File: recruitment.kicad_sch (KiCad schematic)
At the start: 1 part

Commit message: inizio progettazione circuito
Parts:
- removed C1: 1F, Capacitor_SMD:C_0805_2012Metric, symbol Device:C
- added J1: Screw_Terminal_01x01, TerminalBlock:TerminalBlock_Altech_AK300-2_P5.00mm, symbol Connector:Screw_Terminal_01x01
- added K1: Relay_SPST-NO, Relay_THT:Relay_1-Form-A_Schrack-RYII_RM5mm, symbol Relay:Relay_SPST-NO
- added R1, R3, R4: R_US, symbol Device:R_US
- added R2: R_Trim, symbol Device:R_Trim
- added U1: ACS780xLRTR-050B, Sensor_Current:Allegro_PSOF-7_4.8x6.4mm_P1.60mm, symbol Sensor_Current:ACS780xLRTR-050B
- added U2: LM317_TO-220, Package_TO_SOT_THT:TO-220-3_Vertical, symbol Regulator_Linear:LM317_TO-220
- added U3: TL084, symbol Amplifier_Operational:TL084
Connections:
- new net: R1.2, R2.1, U2.1 (ADJ)
- new net: J1.1 (Pin_1), U1.6 (IP-)
- new net: K1.13, U1.5 (IP+)
- new net: U3.1, U3.2 (-)
- new net +3.5V: R3.2, R4.1
- new net +5V: R1.1, U1.1 (VCC), U2.2 (VO), U3.4 (V+)
- new net GND: K1.A2, R2.2, R4.2, U1.2 (GND), U1.4 (NC), U1.7 (NC), U3.11 (V-)
- new net VHall: U1.3 (VOUT), U3.3 (+)
- new net VMonitor: U2.3 (VI)
- new net VPower: K1.14
- no-connect marks 0 -> 2
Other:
- note added: "40 mV/A, ip=0 => Vout = Vcc/2 corrente massima 2.8mA"
- note added: "calcolare r1 r2 in base alla corrente assorbita"
- note added: "scegliendo Vpower = 24Volt"

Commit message: giorno 2 : prime prove e footprint
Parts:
- removed R2: R_Trim, symbol Device:R_Trim
- removed U3: TL084, symbol Amplifier_Operational:TL084
- added R2, R5, R6: R_US, Resistor_THT:R_Axial_DIN0204_L3.6mm_D1.6mm_P2.54mm_Vertical, symbol Device:R_US
- added RV2: R_Potentiometer_US, Potentiometer_THT:Potentiometer_ACP_CA9-H2,5_Horizontal, symbol Device:R_Potentiometer_US
- added U4: OP275, symbol Amplifier_Operational:OP275
- R1, R3, R4: footprint (none) -> Resistor_THT:R_Axial_DIN0204_L3.6mm_D1.6mm_P2.54mm_Vertical
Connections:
- net +5V: now also R6.1, U4.8 (V+)
- net GND: now also R3.2, RV2.2, U4.4 (V-); no longer R4.2
- net VPower: now also R2.1
- net at R1.2, U2.1 (ADJ): now also RV2.1
- net at R3.1: now also R4.1, R2.2, U4.2 (-)
- removed net +3.5V: R3.2, R4.1
- new net: R4.2, R5.2, U4.1
- new net: R5.1, R6.2, U4.3 (+)
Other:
- note added: "11k"
- note added: "120k"
- note added: "2.5Volt per massa virtuale finche l'op non va in saturazione"
- note added: "24-48V"
- note added: "V3 = 2-4V"
- note removed: "40 mV/A, ip=0 => Vout = Vcc/2 corrente massima 2.8mA"
- note removed: "scegliendo Vpower = 24Volt"

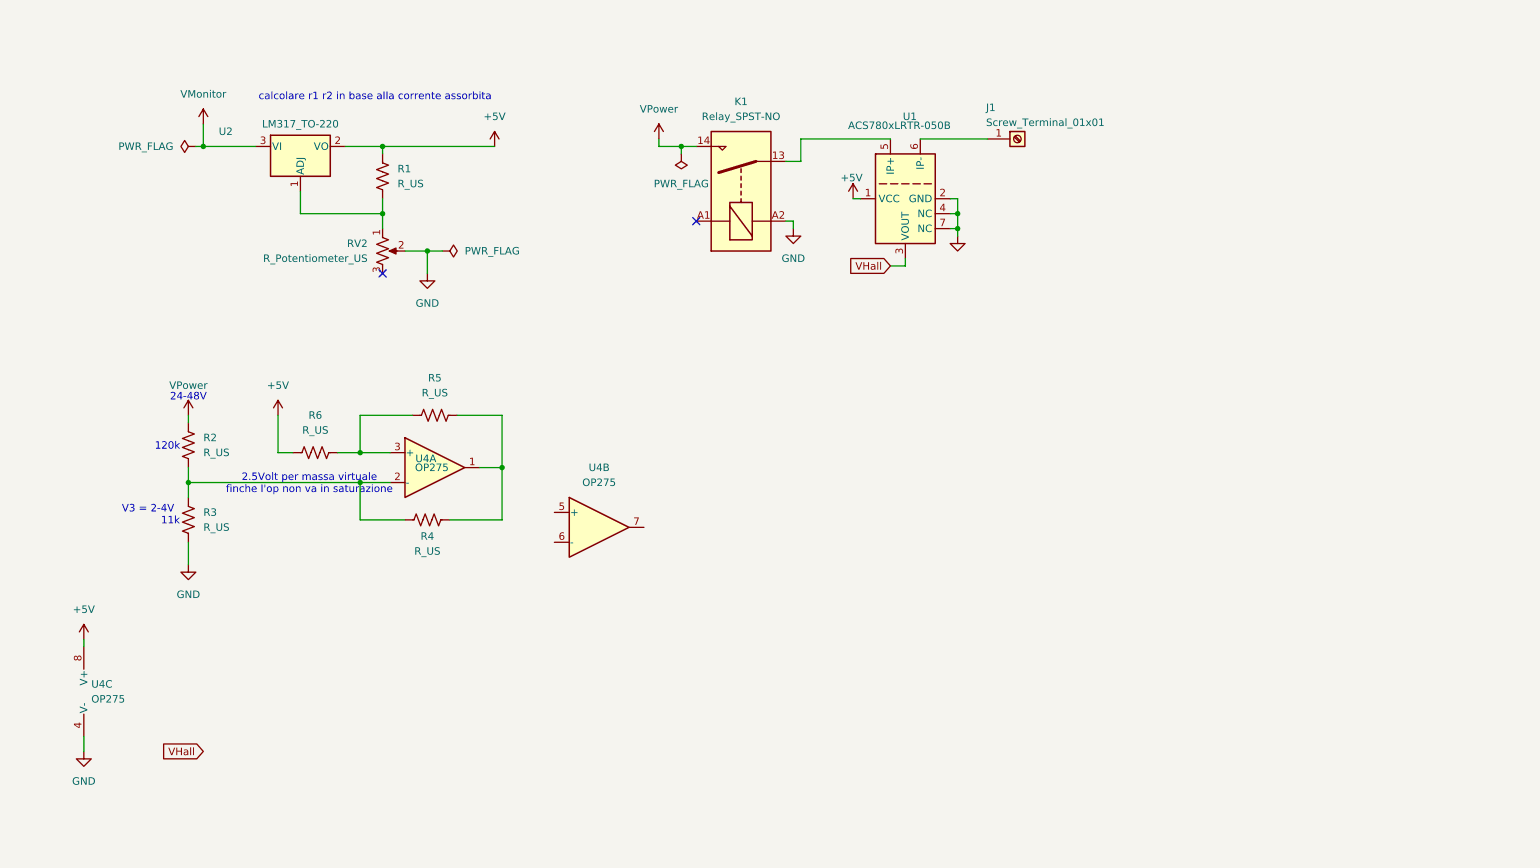
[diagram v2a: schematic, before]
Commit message: continuo schematica, scelta componente latch D
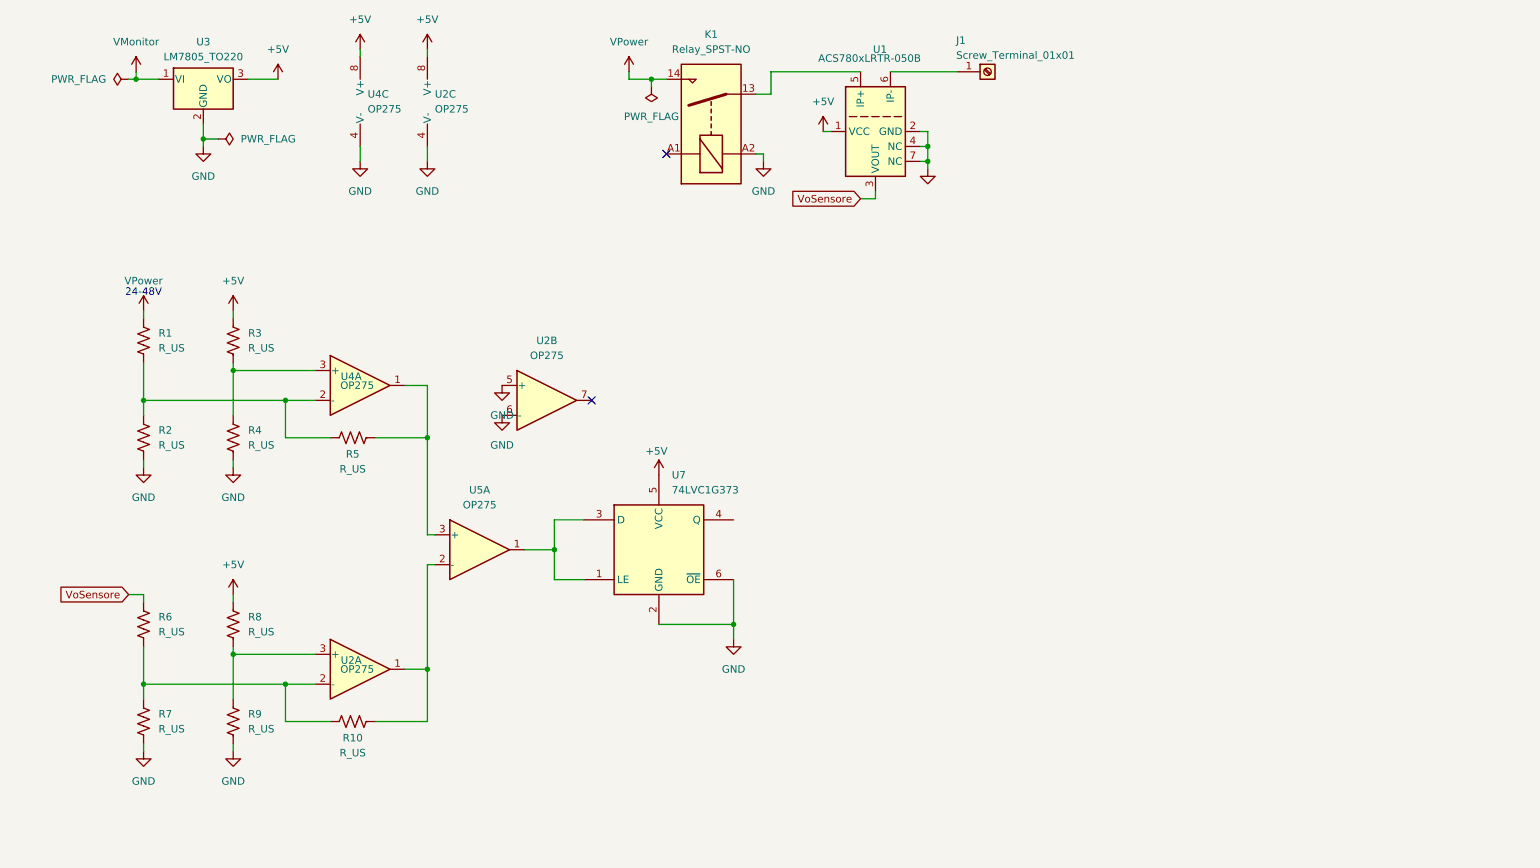
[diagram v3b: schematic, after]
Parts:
- removed R1, R5: R_US, Resistor_THT:R_Axial_DIN0204_L3.6mm_D1.6mm_P2.54mm_Vertical, symbol Device:R_US
- removed RV2: R_Potentiometer_US, Potentiometer_THT:Potentiometer_ACP_CA9-H2,5_Horizontal, symbol Device:R_Potentiometer_US
- removed U2: LM317_TO-220, Package_TO_SOT_THT:TO-220-3_Vertical, symbol Regulator_Linear:LM317_TO-220
- removed unit 2 of U4
- added R10, R4, R6, R7, R8, R9: R_US, Resistor_THT:R_Axial_DIN0204_L3.6mm_D1.6mm_P2.54mm_Vertical, symbol Device:R_US
- added U2, U5: OP275, symbol Amplifier_Operational:OP275
- added U3: LM7805_TO220, Package_TO_SOT_THT:TO-220-3_Vertical, symbol Regulator_Linear:LM7806_TO220
- added U7: 74LVC1G373, symbol 74xGxx:74LVC1G373
- renumbered R2 to R1, R3 to R2, R6 to R3, R4 to R5
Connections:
- net +5V: now also R3.2, R8.2, U2.8 (V+), U3.3 (VO), U7.5 (VCC); no longer R3.1
- net GND: now also R4.2, R7.2, R9.2, U2.4 (V-), U2.5 (+), U2.6 (-), U3.2 (GND), U7.2 (GND), U7.6 (~{OE})
- net VMonitor: now also U3.1 (VI)
- net at R5.2, U4.1: now also U5.3 (+)
- net at U4.3 (+): now also R3.1, R4.1; no longer R3.2
- net VHall renamed VoSensore
- net VoSensore: now also R6.1
- new net: R10.2, U2.1, U5.2 (-)
- new net: R10.1, R6.2, R7.1, U2.2 (-)
- new net: R8.1, R9.1, U2.3 (+)
- new net: U5.1, U7.1 (LE), U7.3 (D)
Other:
- note removed: "11k"
- note removed: "120k"
- note removed: "2.5Volt per massa virtuale finche l'op non va in saturazione"
- note removed: "V3 = 2-4V"
- note removed: "calcolare r1 r2 in base alla corrente assorbita"
- moved on the sheet: J1, K1, R1, R2, R3, R5, U1, U4A, U4C

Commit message: prima prova pcb
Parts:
- removed J1: Screw_Terminal_01x01, TerminalBlock:TerminalBlock_Altech_AK300-2_P5.00mm, symbol Connector:Screw_Terminal_01x01
- removed K1: Relay_SPST-NO, Relay_THT:Relay_1-Form-A_Schrack-RYII_RM5mm, symbol Relay:Relay_SPST-NO
- removed U5: OP275, symbol Amplifier_Operational:OP275
- added J1, J2: ~, TerminalBlock:TerminalBlock_Altech_AK300-2_P5.00mm, symbol Connector:Screw_Terminal_01x02
- added K1: Panasonic_ALFG2PF091, Relay_THT:Relay_SPST_Panasonic_ALFG_FormA_CircularHoles, symbol Relay:Panasonic_ALFG2PF091
- added Q1: IRF9540N, Package_TO_SOT_THT:TO-220-3_Vertical, symbol Transistor_FET:IRF9540N
- added Q2: BC337, Package_TO_SOT_THT:TO-92_Inline, symbol Transistor_BJT:BC337
- added Q3: BC327, Package_TO_SOT_THT:TO-92_Inline, symbol Transistor_BJT:BC327
- added R11, R12, R13, R14: 10k, Resistor_SMD:R_1206_3216Metric, symbol Device:R_US
- added RT1: 10k, Potentiometer_THT:Potentiometer_ACP_CA6-H2,5_Horizontal, symbol Device:R_Potentiometer_Trim_US
- added unit 2 of U3
- R1, R10, R2, R3, R4, R5, R6, R7, R8, R9: footprint Resistor_THT:R_Axial_DIN0204_L3.6mm_D1.6mm_P2.54mm_Vertical -> Resistor_SMD:R_1206_3216Metric
- U2: footprint (none) -> Package_SO:SOIC-8_3.9x4.9mm_P1.27mm
- U3: renamed from U4; footprint (none) -> Package_SO:SOIC-8_3.9x4.9mm_P1.27mm
- U4: renamed from U7; footprint (none) -> Package_TO_SOT_SMD:SOT-23-6
- renumbered U1 to S1, U3 to U1
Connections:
- net GND: now also K1.A2, Q2.3 (E), R13.2, RT1.1; no longer U2.5 (+), U2.6 (-)
- net VMonitor: now also Q1.3 (S), Q3.3 (E), R11.2
- net at R5.2, U3.1: now also U2.5 (+)
- net Load: now reaches S1.6 (IP-)
- net Load: now also J2.2 (Pin_2)
- net at R10.2, U2.1: now also U2.6 (-)
- net at S1.5 (IP+): now also K1.11
- net at U4.1 (LE), U4.3 (D): now also U2.7
- net Shutdown: now reaches U4.4 (Q)
- net Shutdown: now also R12.2
- net VPower renamed Power
- net Power: now also J1.1 (Pin_1), K1.14
- new net: RT1.2, U3.5 (+)
- new net: Q3.1 (C), R13.1, U3.6 (-)
- new net: R14.2, U3.7
- new net: Q2.1 (C), Q3.2 (B), R11.1
- new net: Q2.2 (B), R12.1
- new net: J1.2 (Pin_2), J2.1 (Pin_1)
- new net: Q1.1 (G), R14.1
- new net relé_bobina: K1.A1, Q1.2 (D), RT1.3
- no-connect marks 2 -> 0
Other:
- moved on the sheet: R1, R10, R2, R3, R4, R5, R6, R7, R8, R9, S1, U1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

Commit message: V1.0.0 : prima versione (si spera) funzionante
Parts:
- R1: value R_US -> 120k
- R10: value R_US -> 51k
- R2: value R_US -> 11k
- R3: value R_US -> 6.8k
- R4, R5, R6: value R_US -> 10k
- R7: value R_US -> 51
- R8, R9: value R_US -> 20k
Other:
- title: Template -> Test d'ingresso
- moved on the sheet: J1, J2, K1, Q1, Q2, Q3, R11, R12, R13, R14, RT1, S1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

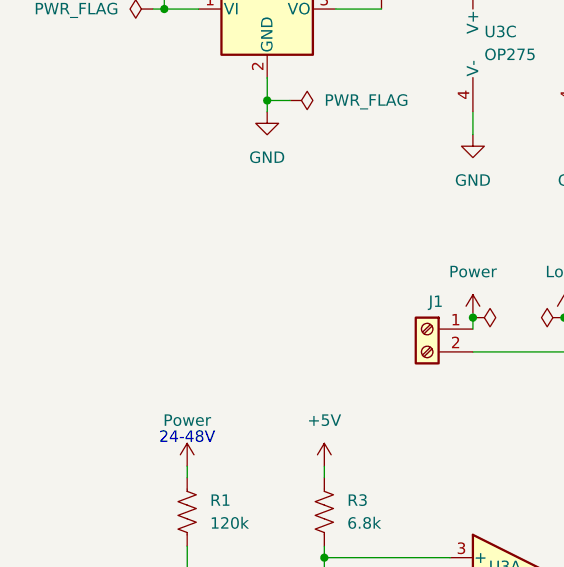
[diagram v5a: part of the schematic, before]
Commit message: Aggiunto pin d'ingresso per Vmonitor, due diversi al posto di una per due perche mi dava problemi sulle distanze minime.
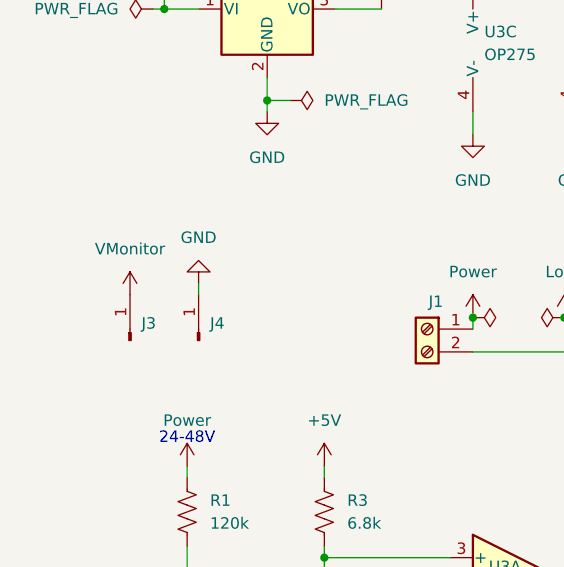
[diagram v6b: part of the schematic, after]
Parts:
- added J3, J4: Conn_01x01_Pin, Connector_PinHeader_1.00mm:PinHeader_1x01_P1.00mm_Vertical, symbol Connector:Conn_01x01_Pin
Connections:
- net GND: now also J4.1 (Pin_1)
- net VMonitor: now also J3.1 (Pin_1)
